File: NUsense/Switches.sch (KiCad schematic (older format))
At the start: 45 parts, among them Q401 2N3055, SW401 SW_SPST, SW402 SW_Push, SW403 SW_Push, U401 ADM6713RAKS, U402 MAX31760

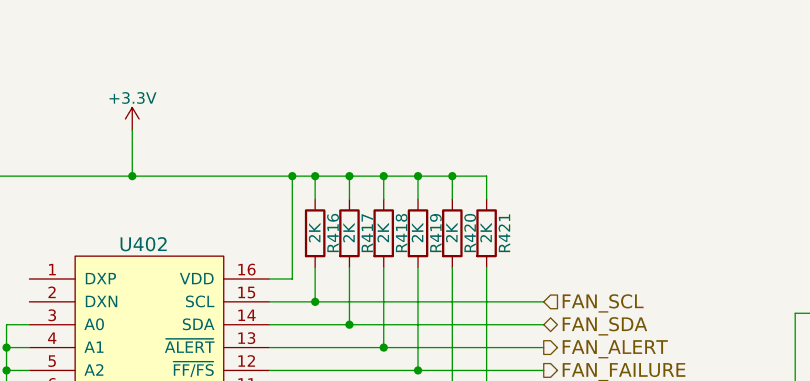
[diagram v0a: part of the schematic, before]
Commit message: Add labels
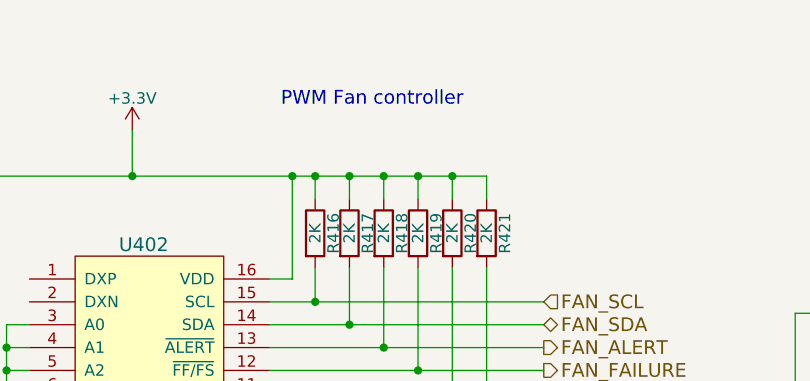
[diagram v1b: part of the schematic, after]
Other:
- note added: "PWM Fan controller"
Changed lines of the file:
@@
 Wire Wire Line
 	2000 3650 2000 3700
+Text Notes 7700 1150 0    60   ~ 0
+PWM Fan controller
 $EndSCHEMATC
